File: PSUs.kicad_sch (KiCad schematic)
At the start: 27 parts, among them J2 Barrel_Jack, J6 SS-52400-004, U3 HUSB238_xxxDD, U4 AP62300WU-7, U8 AP62300WU-7

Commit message: Added lots and lots of traces in PCB design.
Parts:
- removed J6: SS-52400-004, SS-52400-004 (USB-c connector):STEWART_SS-52400-004 (USB-C), symbol SS-52400-004:SS-52400-004
- added J7: 2036150003 (USB-C_Connector), USB-C:CONN_2036150003_MOL(USB-c_connector), symbol 2026-03-08_10-34-21:2036150003
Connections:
- net CC1_U9: now also J7.A5 (CC1)
- net CC2_U9: now also J7.B5 (CC2)
- net GND: now also J7.A1 (GND), J7.A12 (GND), J7.B1 (GND), J7.B12 (GND), J7.GND1 (GND), J7.GND2 (GND)
- net VBUS_A renamed VIN_U9
- net VIN_U9: now also J7.A4 (VBUS), J7.A9 (VBUS), J7.B4 (VBUS)
- no-connect marks 21 -> 14

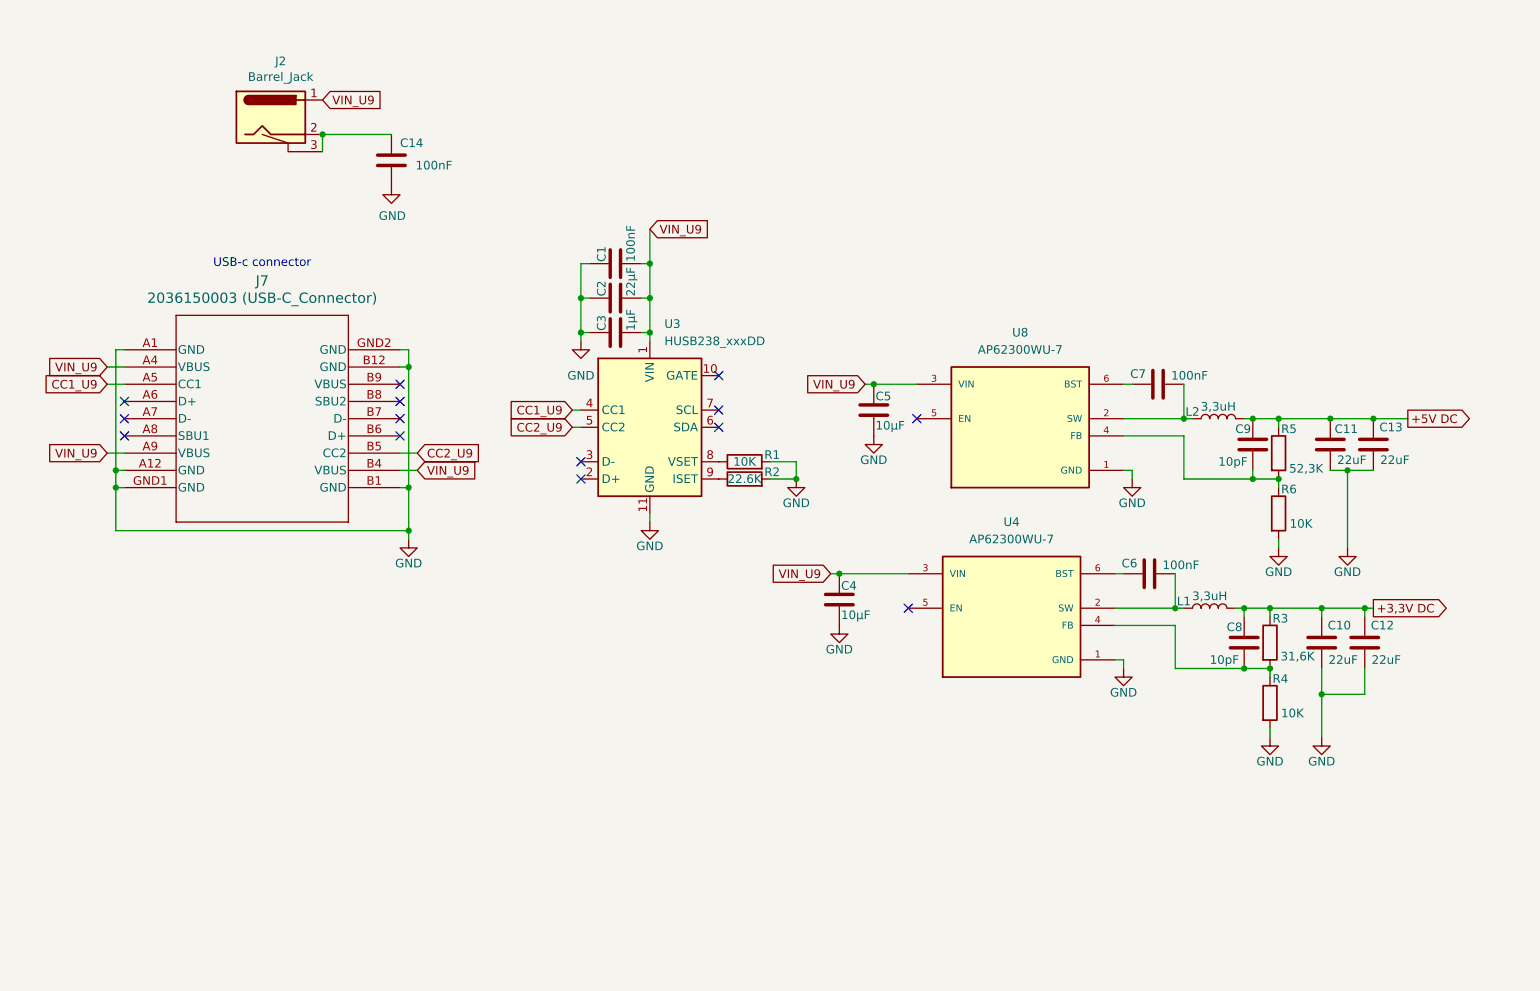
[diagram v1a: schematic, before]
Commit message: Redid the routing and fixed ERC warnings
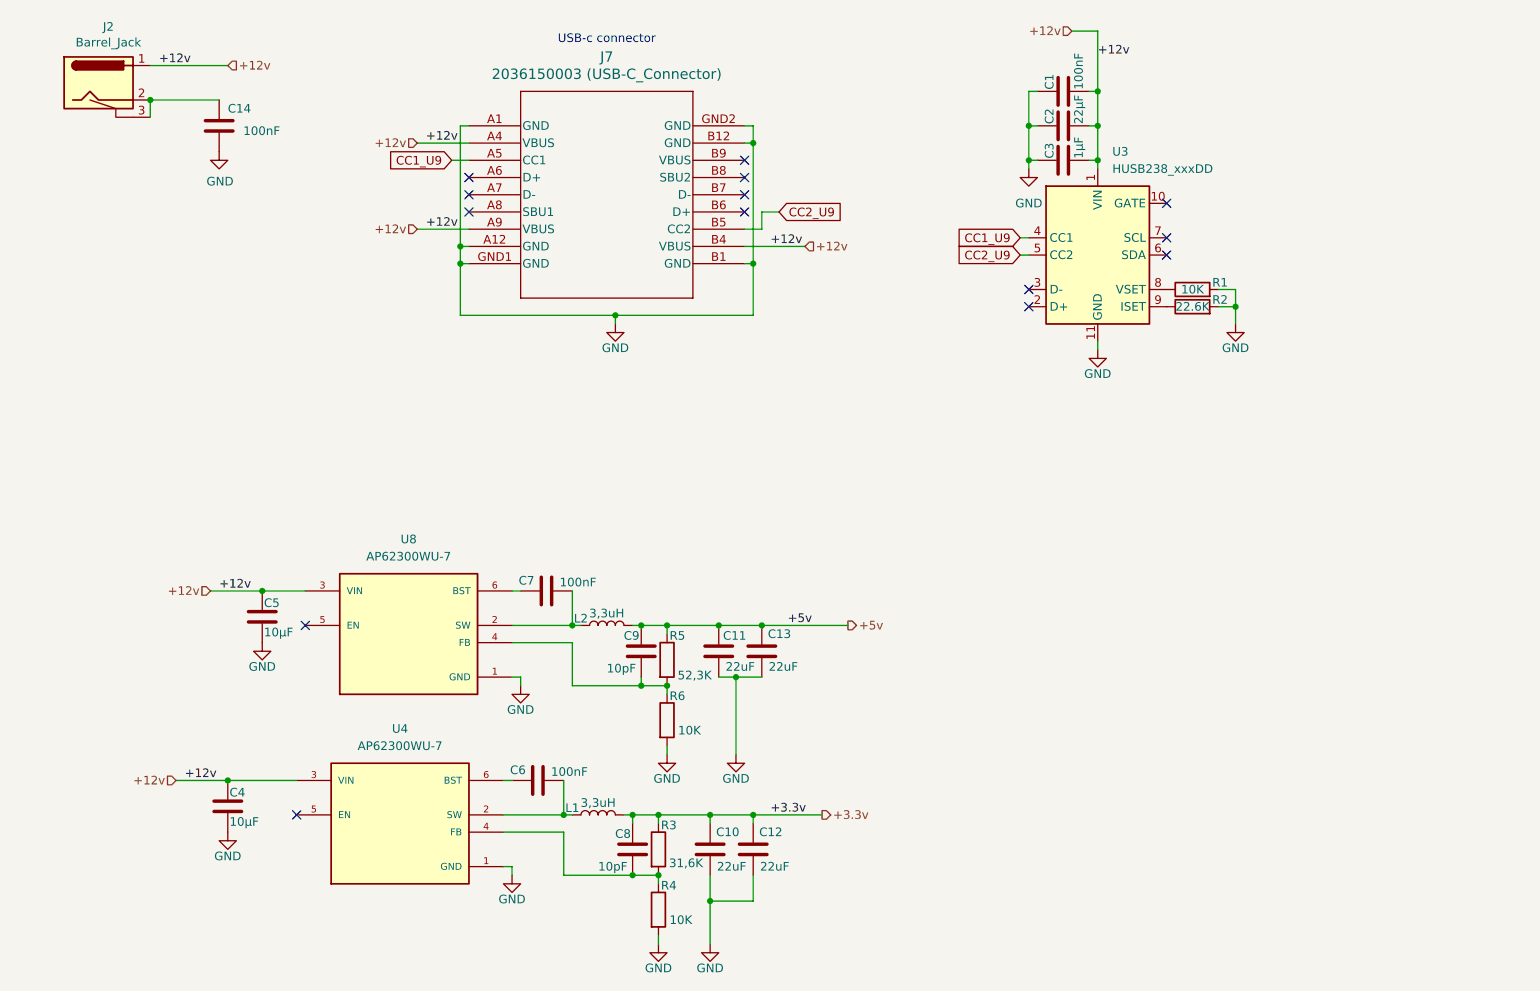
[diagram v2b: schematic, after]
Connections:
- net +3,3V DC renamed +3.3v
- net +5V DC renamed +5v
- net VIN_U9 renamed +12v
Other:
- moved on the sheet: C1, C10, C11, C12, C13, C14, C2, C3, C4, C5, C6, C7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

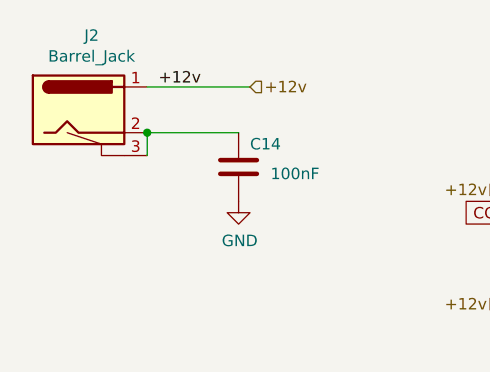
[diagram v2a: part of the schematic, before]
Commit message: Redid traces with correct requirements, needs double checking.
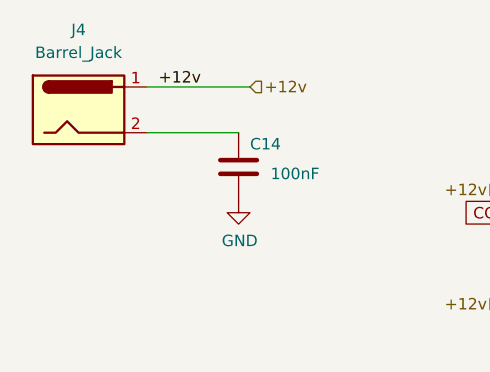
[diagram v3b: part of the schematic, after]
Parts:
- removed J2: Barrel_Jack, Connector_BarrelJack:BarrelJack_CUI_PJ-063AH_Horizontal, symbol CM4IO:Barrel_Jack
- added J4: Barrel_Jack, Connector_BarrelJack:BarrelJack_CUI_PJ-063AH_Horizontal, symbol Connector:Barrel_Jack
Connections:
- net +12v: now also J4.1
- net at C14.1: now also J4.2
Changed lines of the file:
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@@
-	)
-	(junction
-		(at 31.75 25.4)
-		(diameter 0)
-		(color 0 0 0 0)
 	)
 	(junction
@@
 		(pts
 			(xy 114.3 130.81) (xy 120.65 130.81)
-		)
-		(stroke
-			(width 0)
-			(type default)
-		)
-	)
-	(wire
-		(pts
-			(xy 31.75 25.4) (xy 31.75 27.94)
 		)
 		(stroke
@@
 	)
 	(symbol
-		(lib_id "CM4IO:Barrel_Jack")
-		(at 24.13 22.86 0)
-		(unit 1)
-		(exclude_from_sim no)
-		(in_bom yes)
-		(on_board yes)
-		(dnp no)
-		(property "Reference" "J2"
-			(at 25.5778 14.605 0)
-			(effects
-				(font
-					(size 1.27 1.27)
-				)
-			)
-		)
-		(property "Value" "Barrel_Jack"
-			(at 25.5778 16.9164 0)
-			(effects
-				(font
-					(size 1.27 1.27)
-				)
-			)
-		)
-		(property "Footprint" "Connector_BarrelJack:BarrelJack_CUI_PJ-063AH_Horizontal"
-			(at 25.4 23.876 0)
-			(effects
-				(font
-					(size 1.27 1.27)
-				)
-				(hide yes)
-			)
-		)
-		(property "Datasheet" "https://www.toby.co.uk/uploads/publications/842.pdf"
-			(at 25.4 23.876 0)
-			(effects
-				(font
-					(size 1.27 1.27)
-				)
-				(hide yes)
-			)
-		)
-		(property "Description" ""
-			(at 24.13 22.86 0)
-			(effects
-				(font
-					(size 1.27 1.27)
-				)
-			)
-		)
-		(property "Field4" "Toby"
-			(at 24.13 22.86 0)
-			(effects
-				(font
-					(size 1.27 1.27)
-				)
-				(hide yes)
-			)
-		)
-		(property "Field5" "DC-001-A-2.1mm-R"
-			(at 24.13 22.86 0)
-			(effects
-				(font
-					(size 1.27 1.27)
-				)
-				(hide yes)
-			)
-		)
-		(property "Part Description" "DC Power Connectors PCB 2.1MM"
-			(at 24.13 22.86 0)
-			(effects
-				(font
-					(size 1.27 1.27)
-				)
-				(hide yes)
-			)
-		)
-		(property "Field6" "DC-001-A-2.1mm-R"
-			(at 24.13 22.86 0)
-			(effects
-				(font
-					(size 1.27 1.27)
-				)
-				(hide yes)
-			)
-		)
-		(property "Field7" "Valcon"
-			(at 24.13 22.86 0)
-			(effects
-				(font
-					(size 1.27 1.27)
-				)
-				(hide yes)
-			)
-		)
-		(pin "1"
-		)
-		(pin "2"
-		)
-		(pin "3"
-		)
-		(instances
-			(project "ANE21_PCB"
-				(path "/27bae9d5-8d47-4d02-9c9d-2650041a529b/1710a55d-c4fa-4b6a-99e2-6054aab87aa6"
-					(reference "J2")
-					(unit 1)
-				)
-			)
-		)
-	)
-	(symbol
 		(lib_id "Device:R")
 		(at 107.95 116.84 0)
@@
 					(unit 1)
 				)
+			)
+		)
+	)
+	(symbol
+		(lib_id "Connector:Barrel_Jack")
+		(at 24.13 22.86 0)
+		(unit 1)
+		(exclude_from_sim no)
+		(in_bom yes)
+		(on_board yes)
+		(dnp no)
+		(fields_autoplaced yes)
+		(property "Reference" "J4"
+			(at 24.13 13.97 0)
+			(effects
+				(font
+					(size 1.27 1.27)
+				)
+			)
+		)
+		(property "Value" "Barrel_Jack"
+			(at 24.13 16.51 0)
+			(effects
+				(font
+					(size 1.27 1.27)
+				)
+			)
+		)
+		(property "Footprint" "Connector_BarrelJack:BarrelJack_CUI_PJ-063AH_Horizontal"
+			(at 25.4 23.876 0)
+			(effects
+				(font
+					(size 1.27 1.27)
+				)
+				(hide yes)
+			)
+		)
+		(property "Datasheet" "~"
+			(at 25.4 23.876 0)
+			(effects
+				(font
+					(size 1.27 1.27)
+				)
+				(hide yes)
+			)
+		)
+		(property "Description" "DC Barrel Jack"
+			(at 24.13 22.86 0)
+			(effects
+				(font
+					(size 1.27 1.27)
+				)
+				(hide yes)
+			)
+		)
+		(pin "1"
+		)
+		(pin "2"
+		)
+		(instances
+			(project ""
+				(path "/27bae9d5-8d47-4d02-9c9d-2650041a529b/1710a55d-c4fa-4b6a-99e2-6054aab87aa6"
+					(reference "J4")
+					(unit 1)
+				)

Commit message: Hehe, smol board now
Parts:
- removed C14: 100nF, Capacitor_SMD:C_0402_1005Metric_Pad0.74x0.62mm_HandSolder, symbol Device:C
- removed J4: Barrel_Jack, Connector_BarrelJack:BarrelJack_CUI_PJ-063AH_Horizontal, symbol Connector:Barrel_Jack

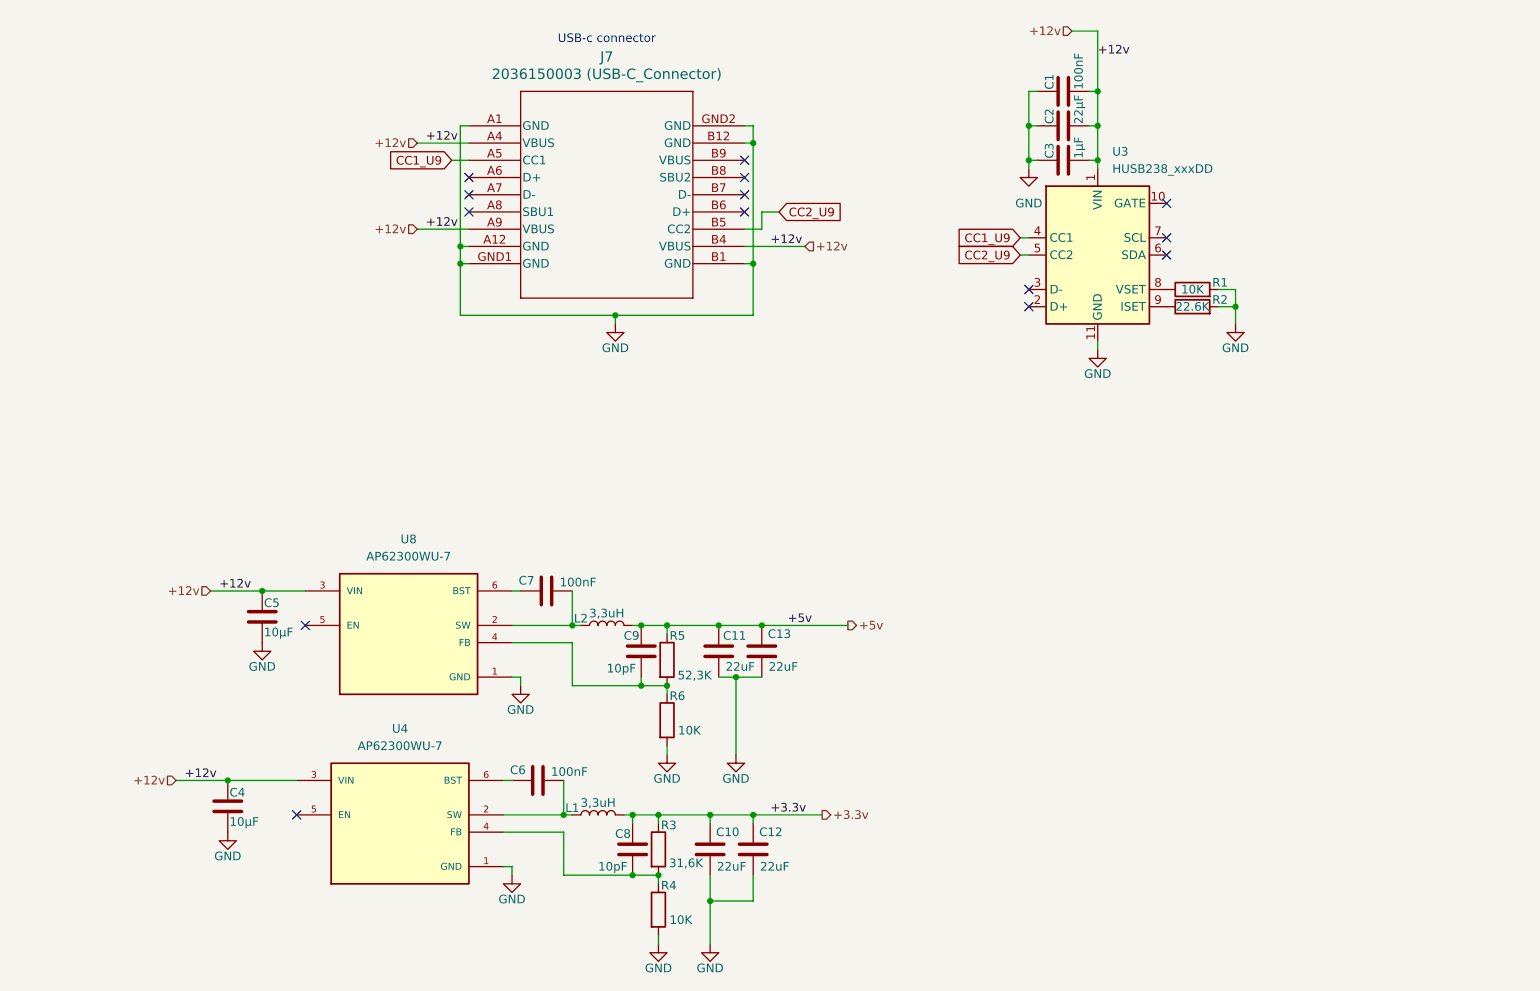
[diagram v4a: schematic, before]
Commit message: Changed quite a bit, PCB smoll now
Redid all traces, replaced HUSB238 with ch224k, made PCB even smaller.
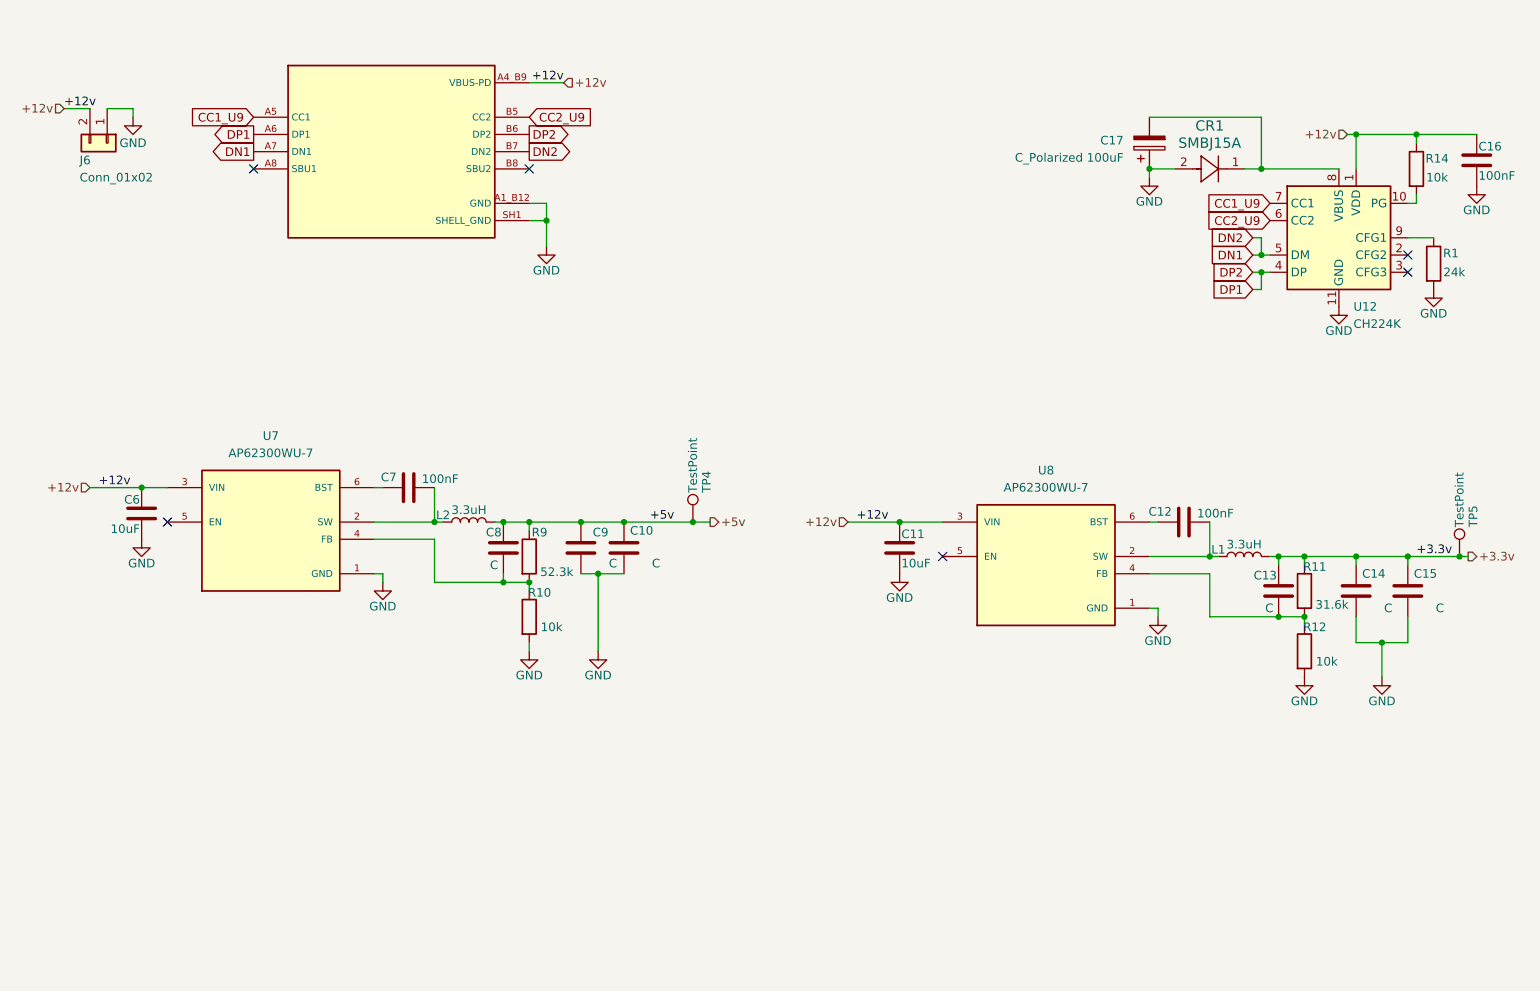
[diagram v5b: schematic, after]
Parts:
- removed C1: 100nF, Capacitor_SMD:C_0402_1005Metric_Pad0.74x0.62mm_HandSolder, symbol Device:C
- removed C2: 22µF, Capacitor_SMD:C_0402_1005Metric_Pad0.74x0.62mm_HandSolder, symbol Device:C
- removed C3: 1µF, Capacitor_SMD:C_0402_1005Metric_Pad0.74x0.62mm_HandSolder, symbol Device:C
- removed J7: 2036150003 (USB-C_Connector), USB-C:CONN_2036150003_MOL(USB-c_connector), symbol 2026-03-08_10-34-21:2036150003
- removed R2: 22.6K, Resistor_SMD:R_0402_1005Metric_Pad0.72x0.64mm_HandSolder, symbol Device:R
- removed U3: HUSB238_xxxDD, Package_DFN_QFN:WDFN-10-1EP_3x3mm_P0.5mm_EP1.8x2.5mm, symbol Interface_USB:HUSB238_xxxDD
- added C16: 100nF, Capacitor_SMD:C_0402_1005Metric_Pad0.74x0.62mm_HandSolder, symbol Device:C
- added C17: C_Polarized 100uF, Capacitor_SMD:CP_Elec_4x3, symbol Device:C_Polarized
- added CR1: SMBJ15A, DIODE_DO214AA, symbol SMBJ15A:SMBJ15A
- added J6: Conn_01x02, TerminalBlock_Phoenix:TerminalBlock_Phoenix_MKDS-1,5-2-5.08_1x02_P5.08mm_Horizontal, symbol Connector_Generic:Conn_01x02
- added R14: 10k, Resistor_SMD:R_0402_1005Metric_Pad0.72x0.64mm_HandSolder, symbol Device:R
- added TP4, TP5: TestPoint, TestPoint:TestPoint_Pad_2.0x2.0mm, symbol Connector:TestPoint
- added U11: ~, symbol USB4105-GF-A:USB4105-GF-A-PD
- added U12: CH224K, Package_SO:SSOP-10-1EP_3.9x4.9mm_P1mm_EP2.1x3.3mm, symbol Interface_USB:CH224K
- C10: renamed from C13; value 22uF -> C
- C11: renamed from C4; value 10µF -> 10uF
- C13: renamed from C8; value 10pF -> C
- C14: renamed from C10; value 22uF -> C
- C15: renamed from C12; value 22uF -> C
- C6: renamed from C5; value 10µF -> 10uF
- C8: renamed from C9; value 10pF -> C
- C9: renamed from C11; value 22uF -> C
- L1, L2: value 3,3uH -> 3.3uH; footprint Inductor_SMD:L_0603_1608Metric -> 1255AY-3R3N_P3:IND_1255AY-3R3N=P3
- R1: value 10K -> 24k
- R10: renamed from R6; value 10K -> 10k
- R11: renamed from R3; value 31,6K -> 31.6k
- R12: renamed from R4; value 10K -> 10k
- R9: renamed from R5; value 52,3K -> 52.3k
- renumbered C6 to C12, U8 to U7, U4 to U8
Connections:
- net +3.3v: now also TP5.1
- net +5v: now also TP4.1
- net CC1_U9: now also U11.A5 (CC1), U12.7 (CC1)
- net CC2_U9: now also U11.B5 (CC2), U12.6 (CC2)
- net GND: now also C16.2, C17.1, CR1.2, J6.1 (Pin_1), U11.A1_B12 (GND), U11.B1_A12 (GND), U11.SH1 (SHELL_GND), U11.SH2 (SHELL_GND), U11.SH3 (SHELL_GND), U11.SH4 (SHELL_GND), U12.11 (GND)
- net at R1.1: now also U12.9 (CFG1)
- net +12v renamed VBUS-PD
- net VBUS-PD: now also C16.1, J6.2 (Pin_2), R14.1, U11.A4_B9 (VBUS-PD), U11.B4_A9 (VBUS-PD), U12.1 (VDD)
- new net: R14.2, U12.10 (PG)
- new net: C17.2, CR1.1, U12.8 (VBUS)
- new net DN1: U11.A7 (DN1), U11.B7 (DN2), U12.5 (DM)
- new net DP1: U11.A6 (DP1), U11.B6 (DP2), U12.4 (DP)
- no-connect marks 14 -> 6
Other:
- note removed: "USB-c connector"
- moved on the sheet: C10, C11, C12, C13, C14, C15, C6, C7, C8, C9, L1, L2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
